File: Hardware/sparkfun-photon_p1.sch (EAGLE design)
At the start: 52 parts, among them U1 WM-N-BM-14

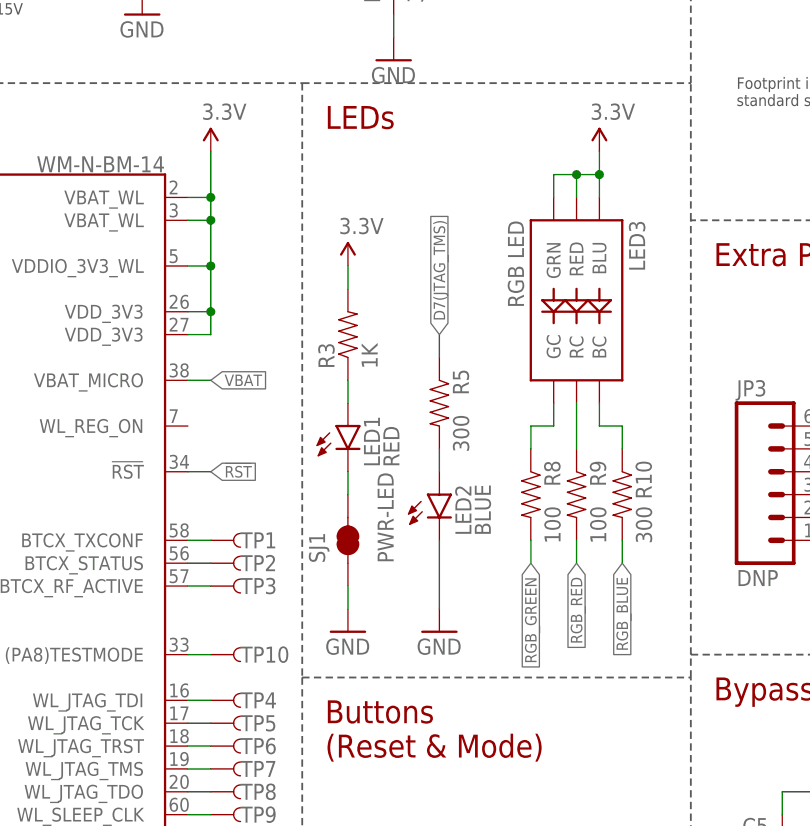
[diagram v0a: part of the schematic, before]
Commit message: Adding jumper to disconnect D7 LED.
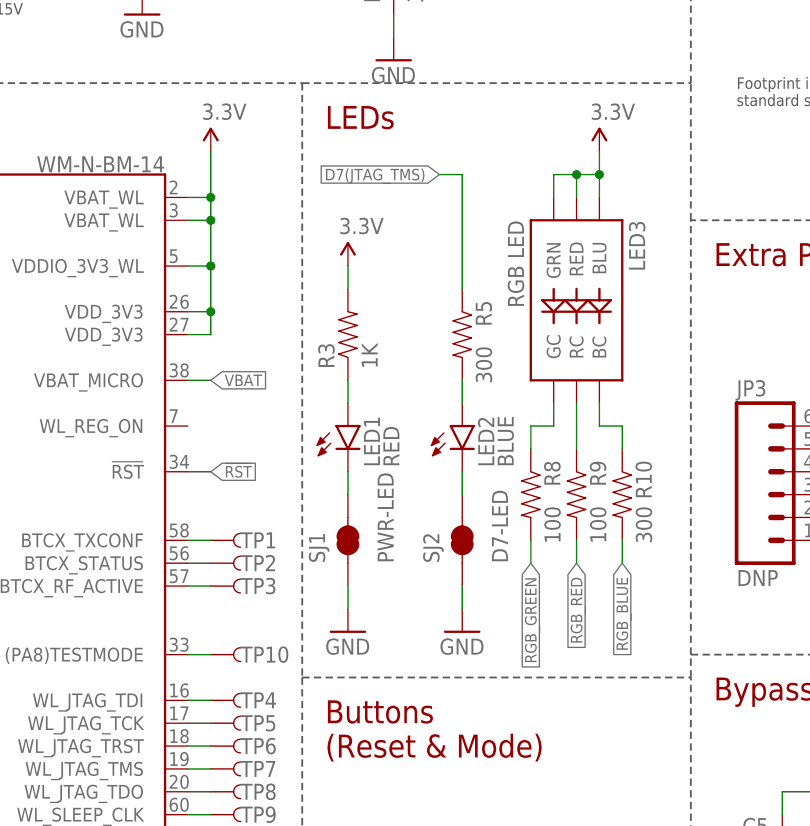
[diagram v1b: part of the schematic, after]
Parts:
- added SJ2: D7-LED, SparkFun-Passives:JUMPER-PAD-2-NC_BY_TRACE
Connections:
- new net N$8: LED2.C, SJ2.2
- net GND: now also SJ2.1; no longer LED2.C
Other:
- moved on the sheet: LED2, R5

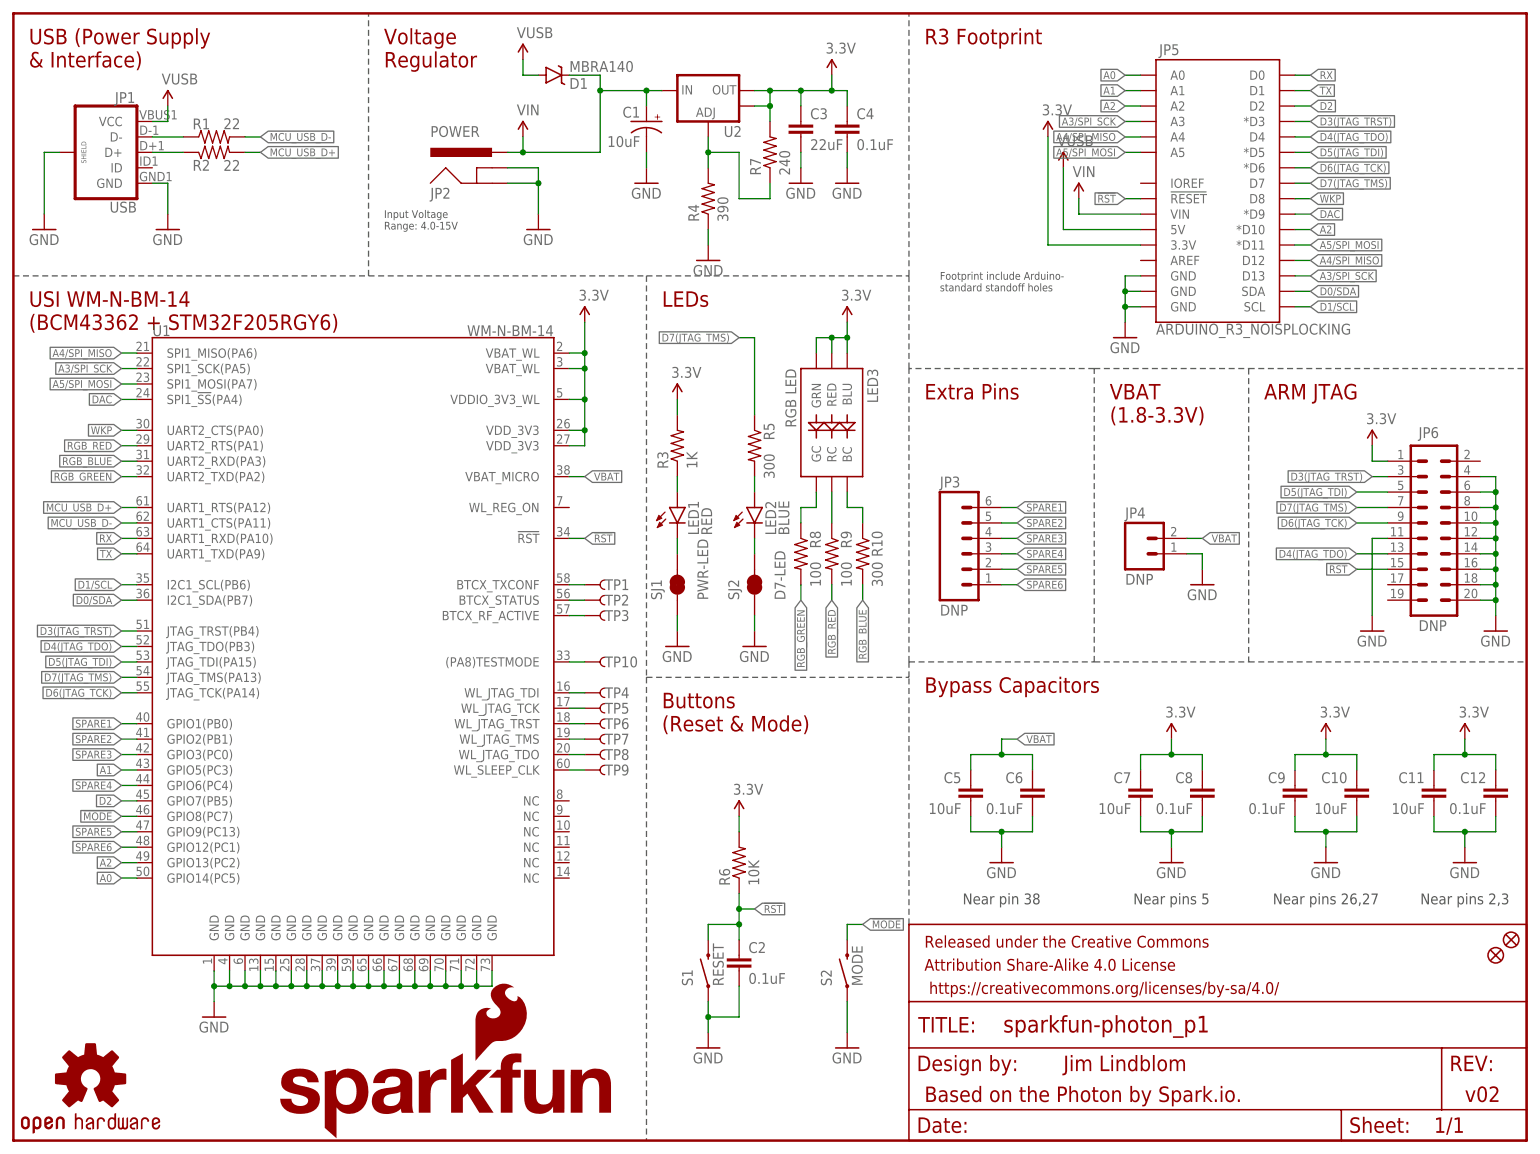
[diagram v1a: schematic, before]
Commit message: Swapping WKP and DAC pins (maps PWM better).
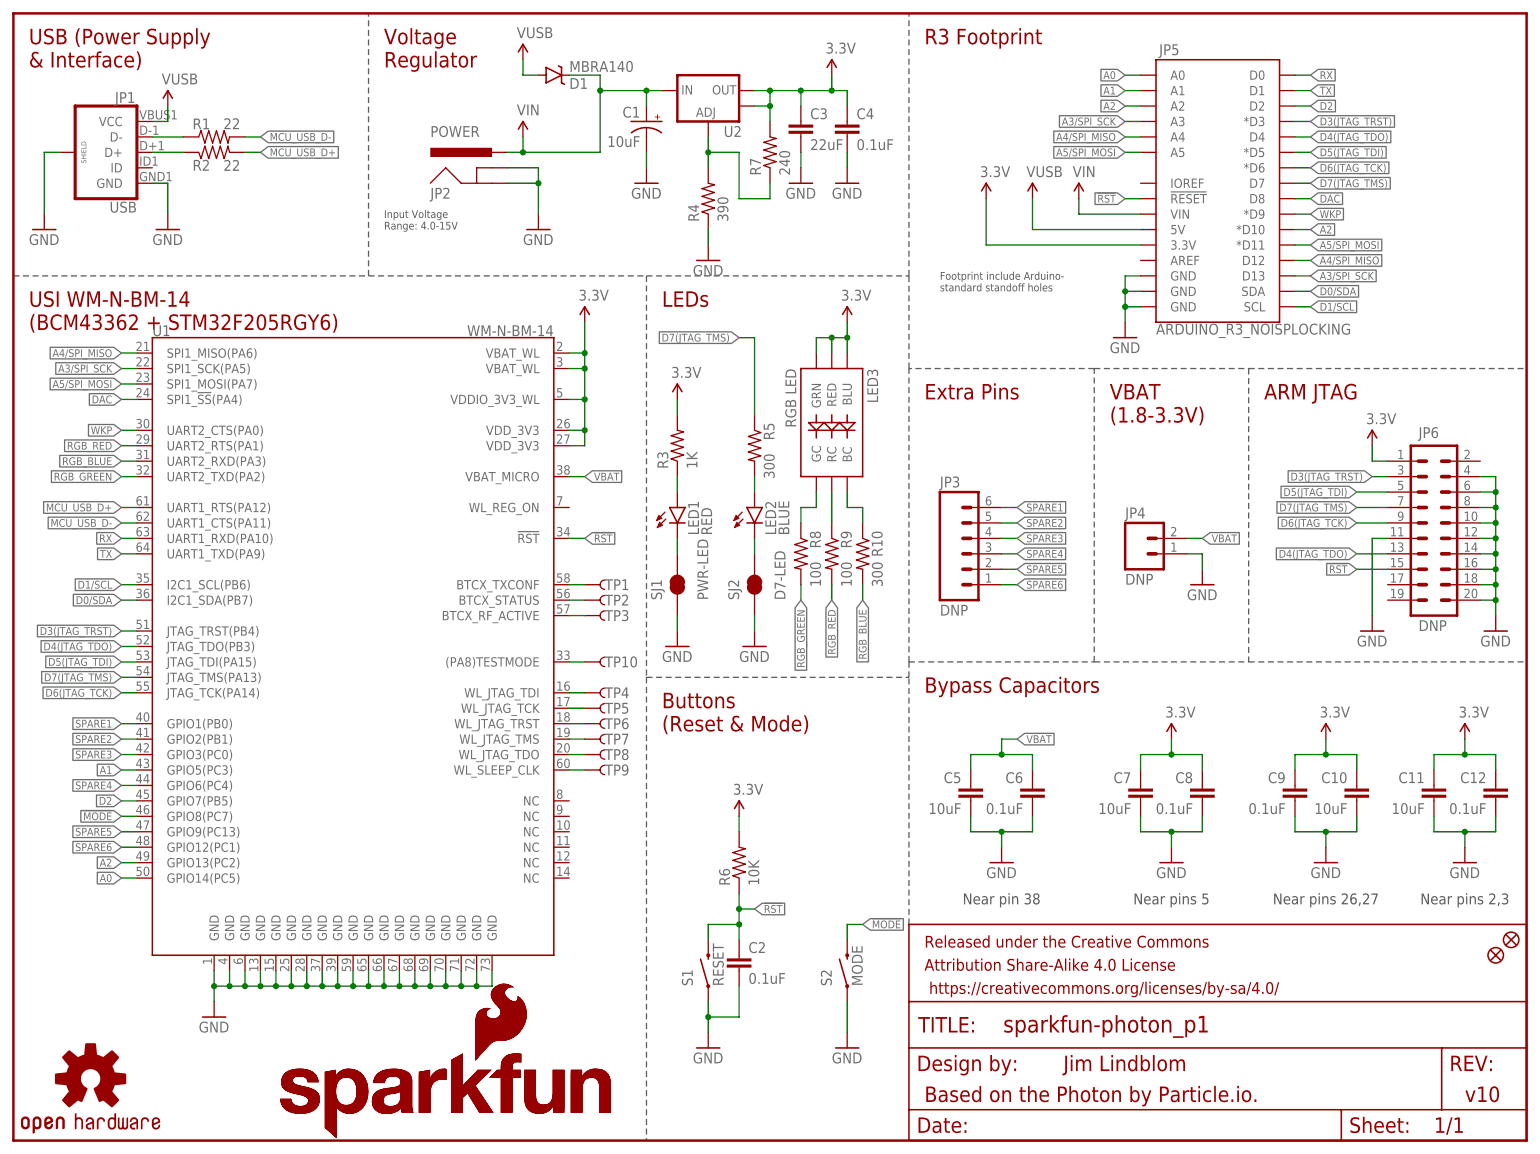
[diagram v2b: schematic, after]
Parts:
- added LOGO3: SFE_LOGO_NAME_FLAME.4_INCH, SparkFun-Aesthetics:SFE_LOGO_NAME_FLAME.4_INCH
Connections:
- net DAC: now also JP5.D8; no longer JP5.*D9
- net WKP: now also JP5.*D9; no longer JP5.D8
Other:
- note added: "Based on the Photon by Particle.io."
- note added: "v10"
- note removed: "Based on the Photon by Spark.io."
- note removed: "v02"

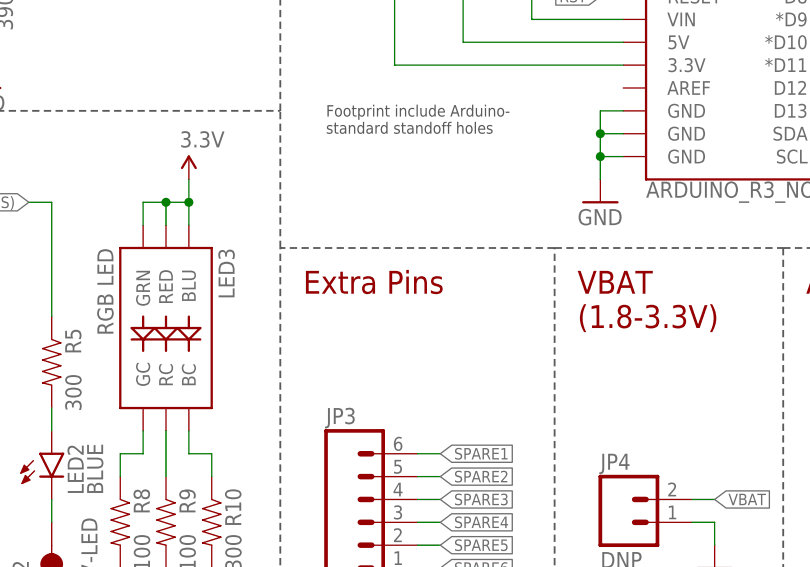
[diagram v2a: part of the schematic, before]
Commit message: Moving vias to avoid silk.
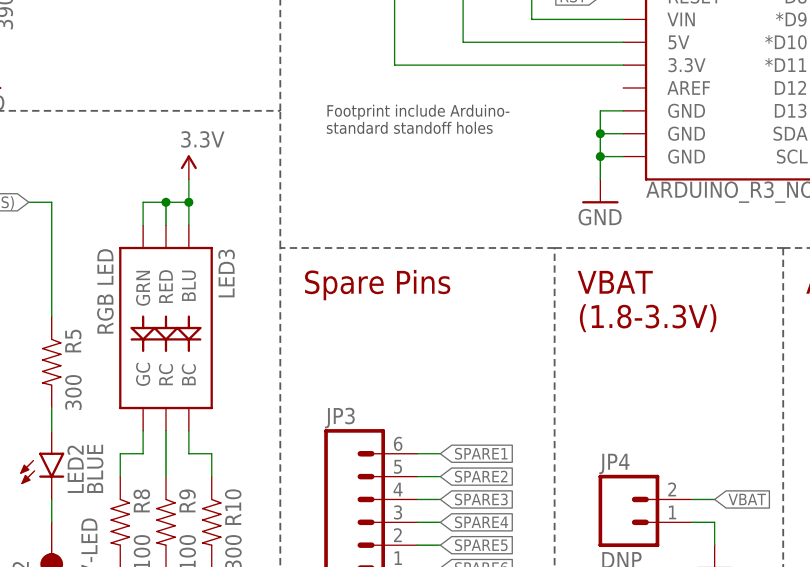
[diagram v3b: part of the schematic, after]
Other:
- note added: "Spare Pins"
- note removed: "Extra Pins"
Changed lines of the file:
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@@
 &amp; Interface)</text>
 <text x="149.86" y="182.88" size="2.54" layer="94" align="top-left">R3 Footprint</text>
-<text x="149.86" y="124.46" size="2.54" layer="94" align="top-left">Extra Pins</text>
+<text x="149.86" y="124.46" size="2.54" layer="94" align="top-left">Spare Pins</text>
 <wire x1="177.8" y1="127" x2="203.2" y2="127" width="0.2032" layer="97" style="shortdash"/>
 <wire x1="203.2" y1="127" x2="248.92" y2="127" width="0.2032" layer="97" style="shortdash"/>
